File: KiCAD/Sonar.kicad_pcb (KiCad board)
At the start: 4 copper layers, 150 x 150 mm, 353 parts, among them J1 DIN-40-Female, J2 DIN-20, SW1 CrossBar, SW10 CrossBar, SW11 CrossBar, SW12 CrossBar, SW13 CrossBar, SW14 CrossBar, SW15 CrossBar, SW16 CrossBar, SW17 CrossBar, SW18 CrossBar, SW19 CrossBar, SW2 CrossBar, SW20 CrossBar, SW21 CrossBar, SW22 CrossBar, SW23 CrossBar, SW24 CrossBar, SW25 CrossBar, SW26 CrossBar, SW27 CrossBar, SW28 CrossBar, SW29 CrossBar, SW3 CrossBar, SW30 CrossBar, SW31 CrossBar, SW32 CrossBar, SW33 CrossBar, SW34 CrossBar, SW35 CrossBar, SW36 CrossBar, SW37 CrossBar, SW38 CrossBar, SW39 CrossBar, SW4 CrossBar, SW40 CrossBar, SW41 CrossBar, SW42 CrossBar, SW43 CrossBar, SW44 CrossBar, SW45 CrossBar, SW46 CrossBar, SW47 CrossBar, SW48 CrossBar, SW49 CrossBar, SW5 CrossBar, SW50 CrossBar, SW51 CrossBar, SW52 CrossBar, SW53 CrossBar, SW54 CrossBar, SW55 CrossBar, SW56 CrossBar, SW57 CrossBar, SW58 CrossBar, SW59 CrossBar, SW6 CrossBar, SW60 CrossBar, SW61 CrossBar, SW62 CrossBar, SW63 CrossBar, SW64 CrossBar, SW7 CrossBar, SW8 CrossBar, SW9 CrossBar, U1 TPA6211A1DRBR, U2 MAX11059, U3 MAX11059, U4 AD8534ARZ-REEL, U5 AD8534ARZ-REEL, U6 AD8534ARZ-REEL, U7 AD8534ARZ-REEL

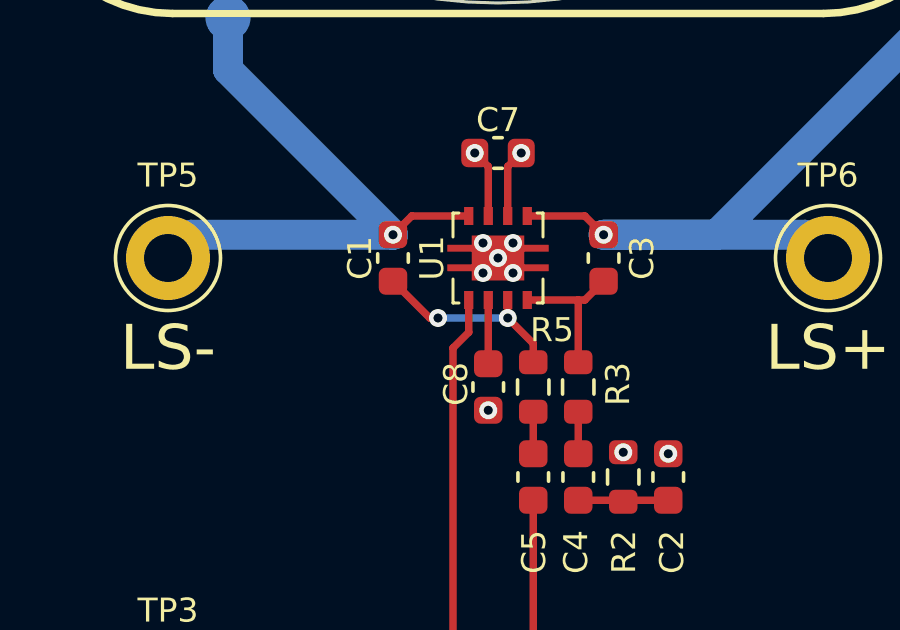
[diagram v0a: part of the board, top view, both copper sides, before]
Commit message: Changed 100pF and 100nF to AVX parts, and gave TPA6211 a pin-1 dot
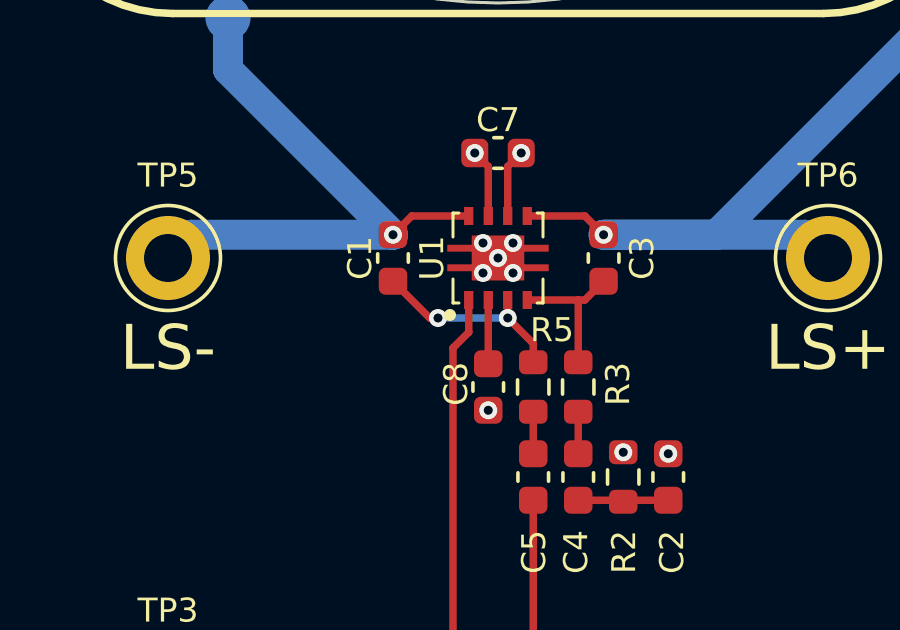
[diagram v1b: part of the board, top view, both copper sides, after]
